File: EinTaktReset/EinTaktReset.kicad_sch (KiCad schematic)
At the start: 44 parts, among them J1 Conn_01x02, J2 Conn_01x03, J3 Conn_01x03, J4 Conn_01x03, J5 Conn_01x02, J6 Conn_01x02, J7 Conn_02x03_Odd_Even, P1 CONN_02X10, P4 CONN_02X10, SW1 Digitast, SW10 SPST, SW11 SPST, SW12 SPST, SW13 SPST, SW2 Digitast, SW3 SW_SPDT, SW4 SW_SPDT, SW5 SPST, SW6 SW_SPDT, SW7 SPST, SW8 SPST, SW9 SPST, U2 ATmega48-20P, U3 74HC541, U5 7400, Y1 Crystal

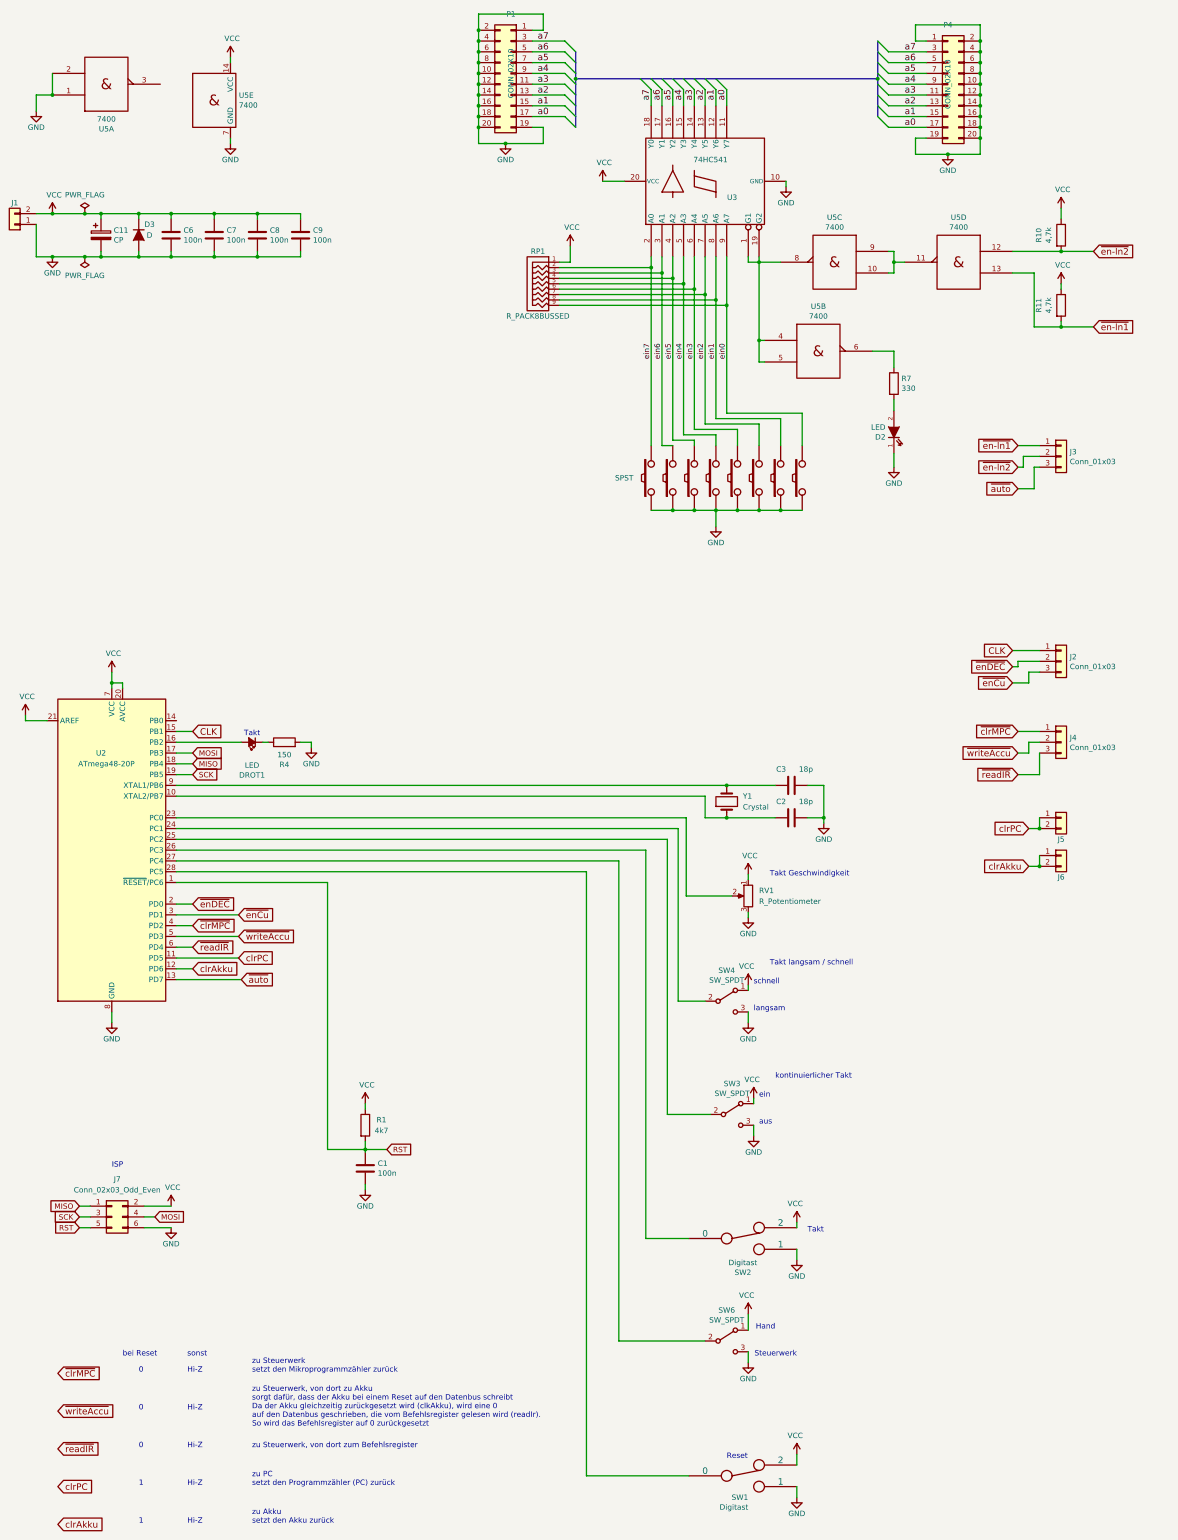
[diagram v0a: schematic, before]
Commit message: - Werte von Bauteilen in den Schaltplänen ergänzt - weitere Hinweise zum Nachbau
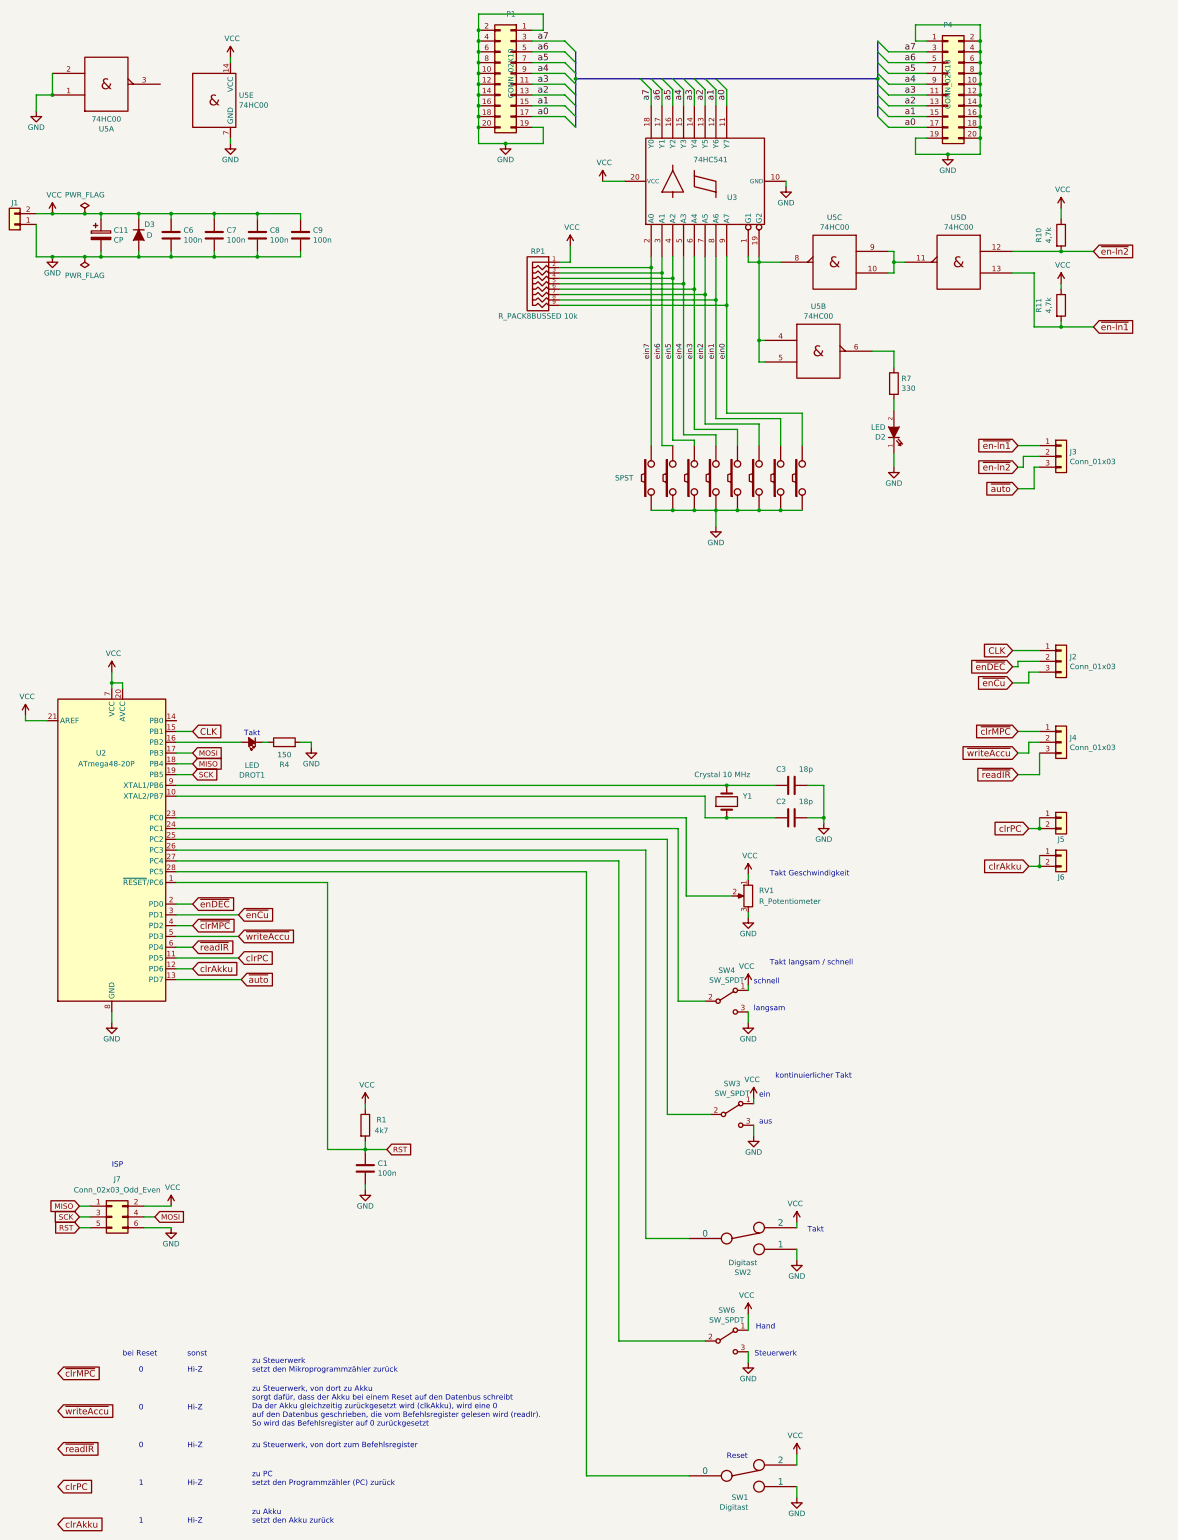
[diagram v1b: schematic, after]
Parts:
- RP1: value R_PACK8BUSSED -> R_PACK8BUSSED 10k
- U5: value 7400 -> 74HC00
- Y1: value Crystal -> Crystal 10 MHz
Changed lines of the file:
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@@
       (effects (font (size 1.27 1.27)))
     )
-    (property "Value" "R_PACK8BUSSED" (at 142.24 87.63 0)
+    (property "Value" "R_PACK8BUSSED 10k" (at 142.24 87.63 0)
       (effects (font (size 1.27 1.27)))
     )
@@
       (effects (font (size 1.27 1.27)))
     )
-    (property "Value" "7400" (at 212.09 66.7004 0)
+    (property "Value" "74HC00" (at 212.09 66.7004 0)
       (effects (font (size 1.27 1.27)))
     )
@@
       (effects (font (size 1.27 1.27)))
     )
-    (property "Value" "7400" (at 241.3 66.7004 0)
+    (property "Value" "74HC00" (at 241.3 66.7004 0)
       (effects (font (size 1.27 1.27)))
     )
@@
       (effects (font (size 1.27 1.27)) (justify left))
     )
-    (property "Value" "7400" (at 71.8312 37.973 0)
+    (property "Value" "74HC00" (at 71.8312 37.973 0)
       (effects (font (size 1.27 1.27)) (justify left))
     )
@@
       (effects (font (size 1.27 1.27)))
     )
-    (property "Value" "7400" (at 208.28 87.6554 0)
+    (property "Value" "74HC00" (at 208.28 87.6554 0)
       (effects (font (size 1.27 1.27)))
     )
@@
   )
   (symbol (lib_id "Device:Crystal") (at 186.69 201.93 90) (unit 1)
-    (in_bom yes) (on_board yes) (dnp no) (fields_autoplaced)
+    (in_bom yes) (on_board yes) (dnp no)
     (property "Reference" "Y1" (at 190.5 200.66 90)
       (effects (font (size 1.27 1.27)) (justify right))
     )
-    (property "Value" "Crystal" (at 190.5 203.2 90)
+    (property "Value" "Crystal 10 MHz" (at 179.07 195.58 90)
       (effects (font (size 1.27 1.27)) (justify right))
     )
@@
       (effects (font (size 1.27 1.27)))
     )
-    (property "Value" "7400" (at 40.64 41.2496 0)
-      (effects (font (size 1.27 1.27)))
-    )
+    (property "Value" "74HC00" (at 40.64 41.2496 0)
+      (effects (font (size 1.27 1.27)))
+    )

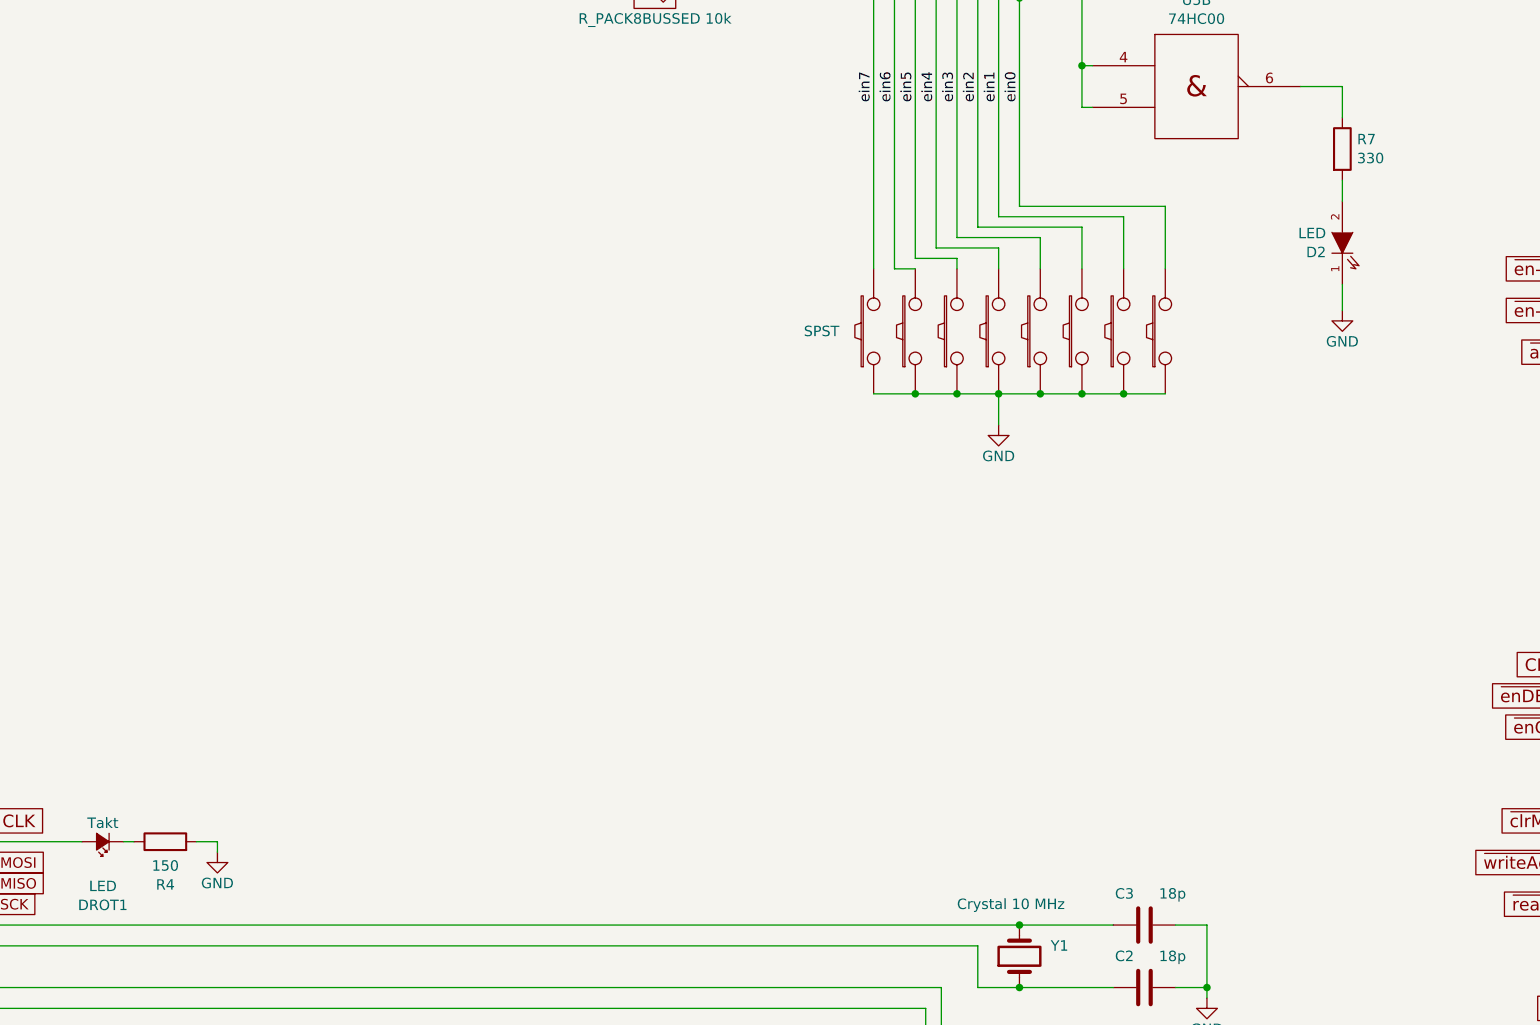
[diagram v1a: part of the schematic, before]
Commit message: Alle Vorwiderstände vor LEDs in 680 Ohm geändert (Issue 5)
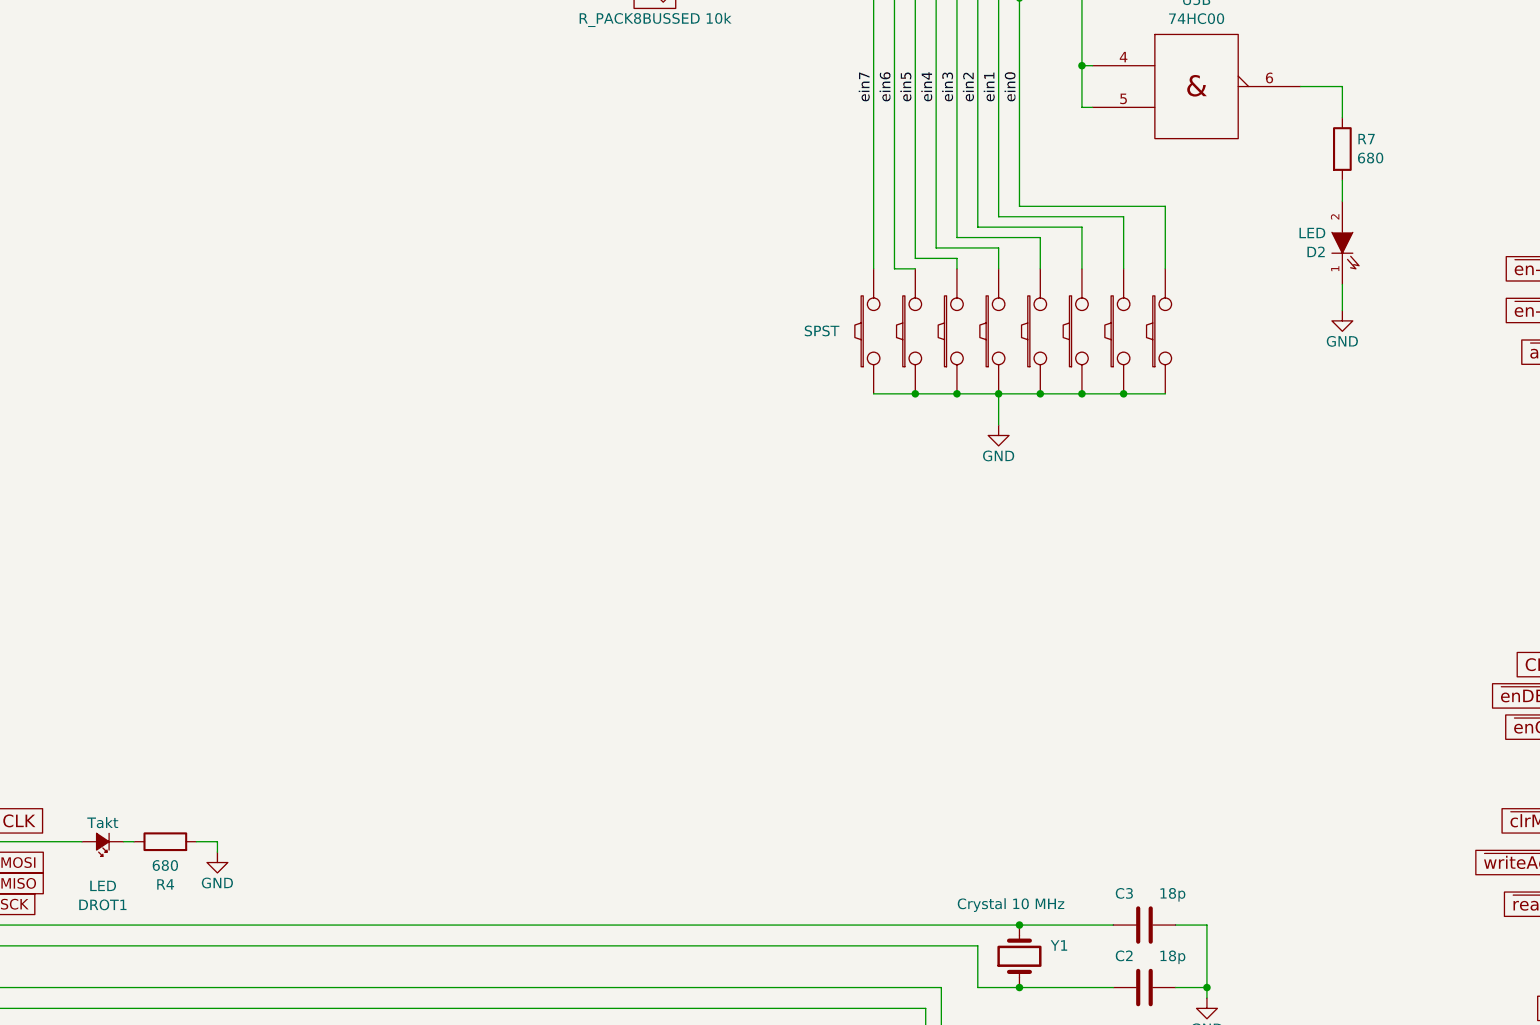
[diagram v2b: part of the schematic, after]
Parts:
- R4: value 150 -> 680
- R7: value 330 -> 680
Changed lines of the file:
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@@
       (effects (font (size 1.27 1.27)) (justify left))
     )
-    (property "Value" "330" (at 227.838 104.648 0)
+    (property "Value" "680" (at 227.838 104.648 0)
       (effects (font (size 1.27 1.27)) (justify left))
     )
@@
       (effects (font (size 1.27 1.27)))
     )
-    (property "Value" "150" (at 82.55 190.9064 90)
+    (property "Value" "680" (at 82.55 190.9064 90)
       (effects (font (size 1.27 1.27)))
     )
